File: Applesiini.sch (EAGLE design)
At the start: 55 parts

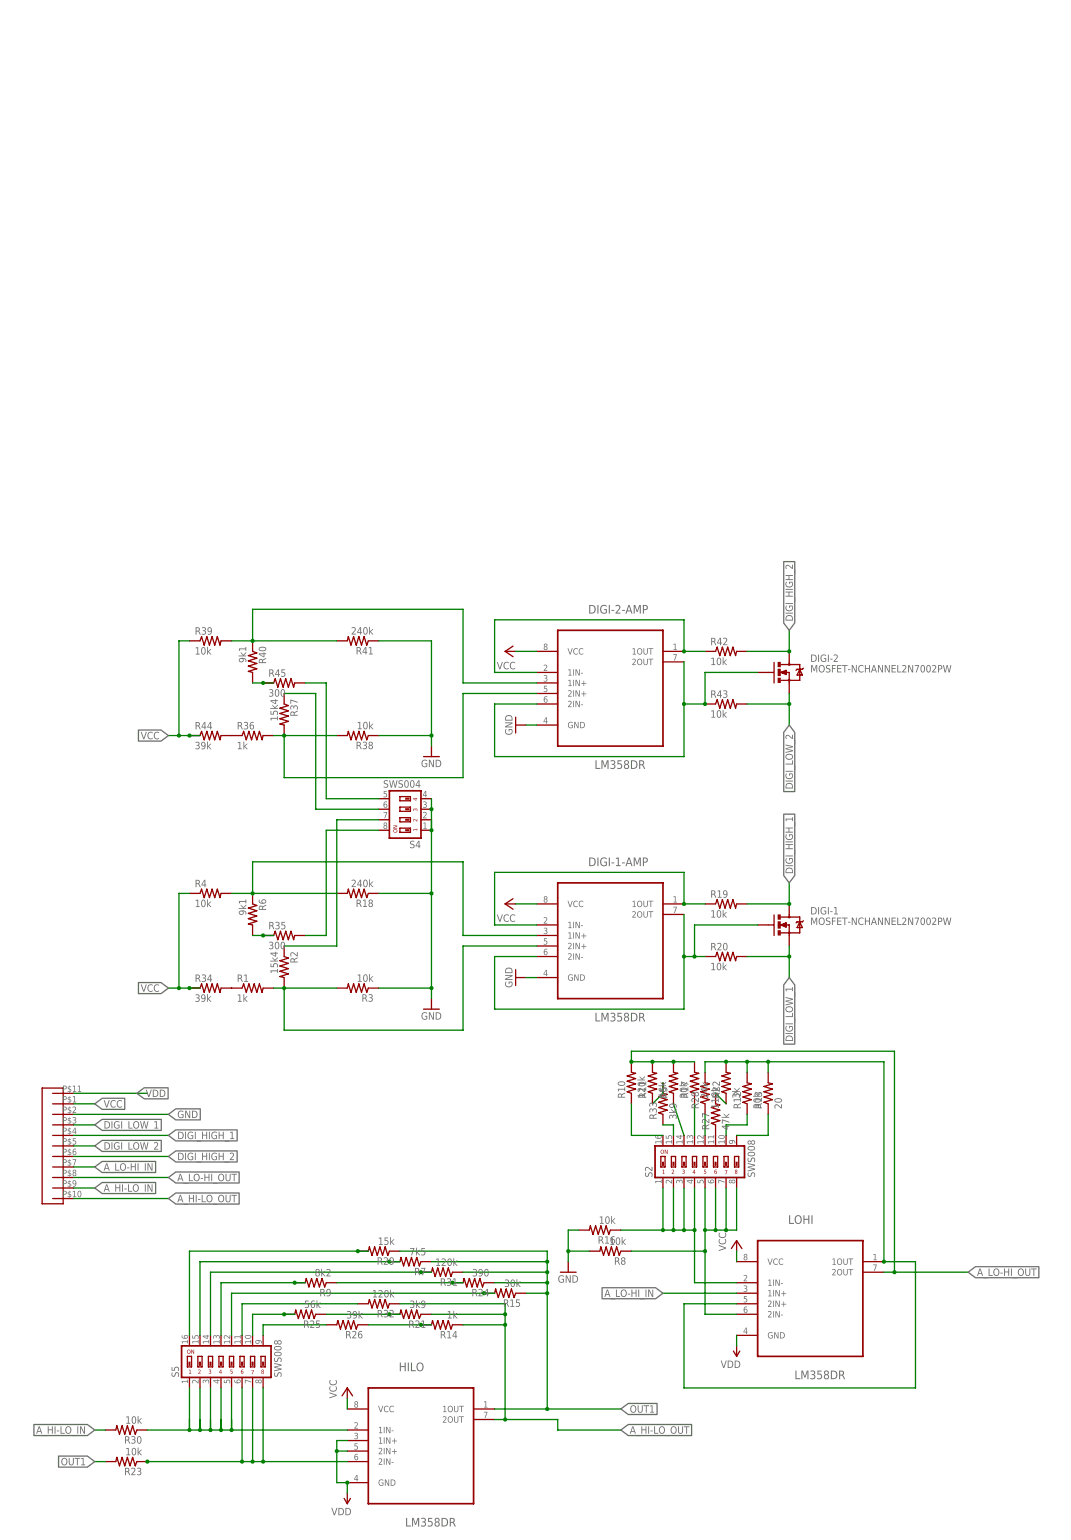
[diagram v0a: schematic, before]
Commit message: begin lime-lemon schematic and board
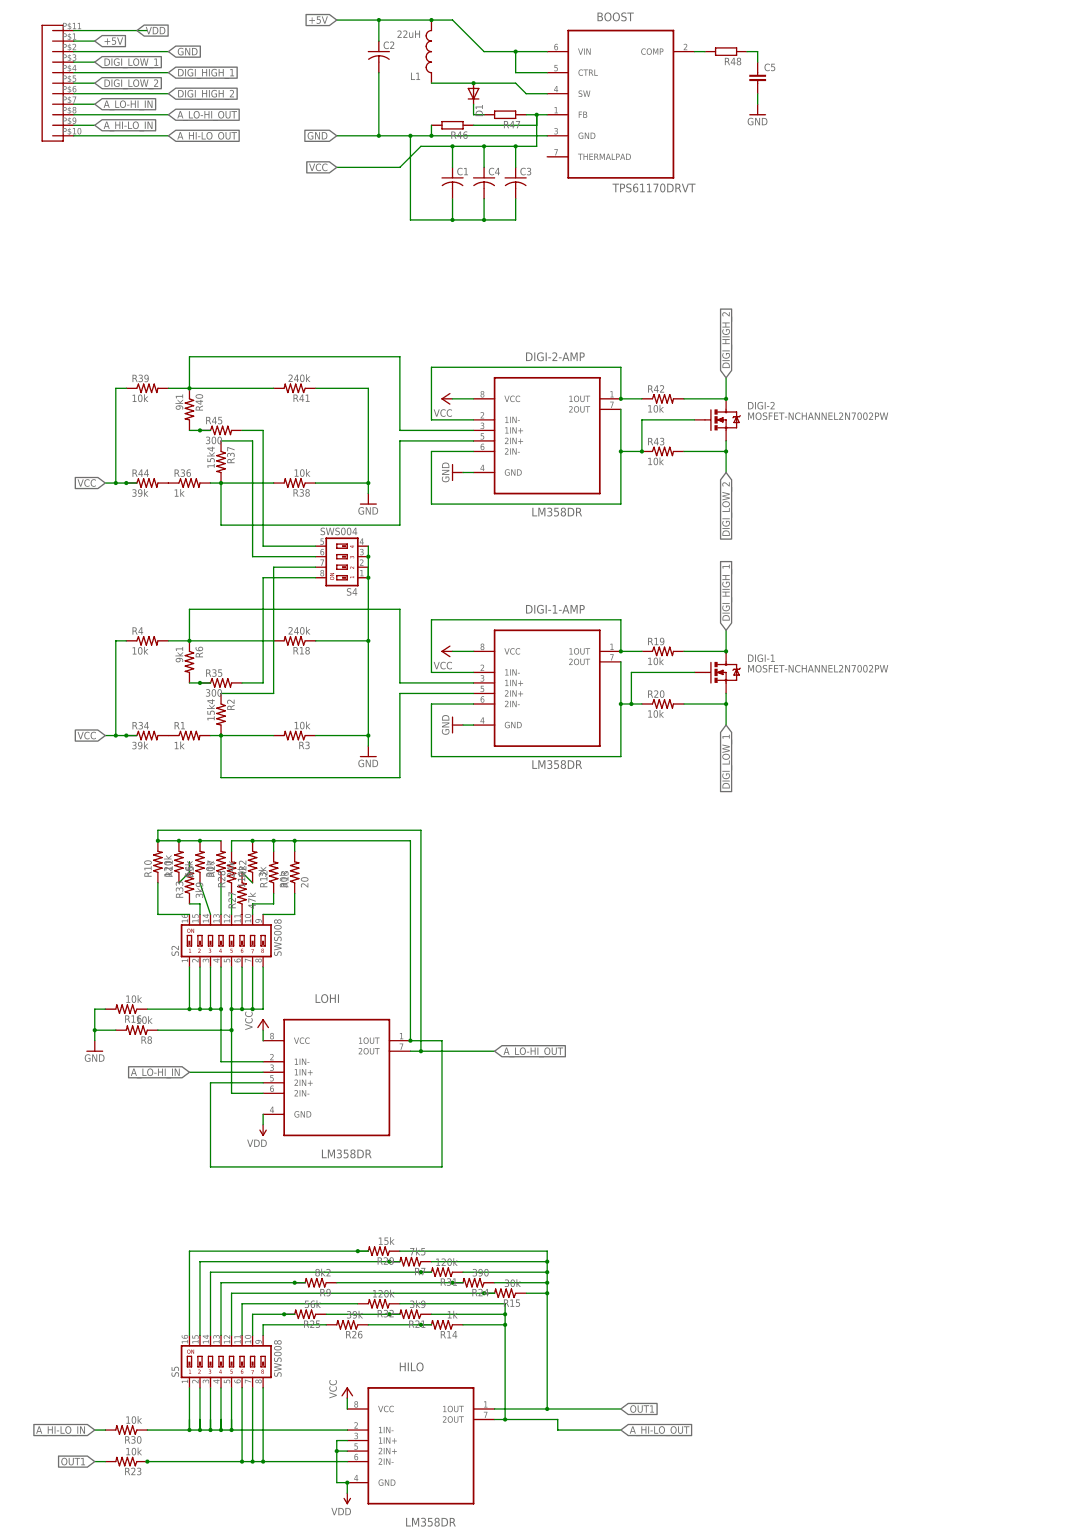
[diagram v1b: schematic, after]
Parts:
- added BOOST: TPS61170DRVT, Texas Instruments_By_element14_Batch_1:TPS61170DRVT
- added C1, C3, C4: (no value), rcl:C-USC1206
- added C2: (no value), rcl:C-USC0805
- added C5: (no value), rcl:C-EUC0805
- added D1: (no value), diode:DIODE-SOD123
- added L1: 22uH, SparkFun-Passives:INDUCTORBOURNS_SRN6045
- added R46, R47, R48: (no value), rcl:R-EU_R0805
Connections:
- new net +5V: BOOST.CTRL, BOOST.VIN, C2.1, L1.2, U$1.P$1
- new net N$44: BOOST.SW, D1.A, L1.1
- new net N$47: D1.C, R47.2
- new net N$49: BOOST.COMP, R48.2
- new net N$51: C5.1, R48.1
- net GND: now also BOOST.GND, C1.2, C2.2, C3.2, C4.2, C5.2, R46.2
- net VCC: now also BOOST.FB, C1.1, C3.1, C4.1, R46.1, R47.1; no longer U$1.P$1
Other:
- moved on the sheet: DIGI-1, DIGI-1-AMP, DIGI-2, DIGI-2-AMP, LOHI, R1, R10, R11, R12, R13, R16, R17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
